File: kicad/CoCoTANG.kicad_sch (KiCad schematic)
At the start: 108 parts, among them J1 CPU, J10 PIA1_OUT, J13 CoCo_Cart, J14 PIA0_IN, J15 PIA1_IN, J17 AV_IN, J18 CMP_IN, J2 ADDRMUX_OUT, J20 AV_OUT, J21 CMP_OUT, J23 TRG, J28 ADDRMUX, J3 ADDRMUX_IN, J4 PIA0, J5 PIA1, J6 CLK, J7 AV_HEADER, J8 PIA0_OUT, Q1 MMBT3904-TP, Q2 MMBT3904-TP, Q3 MMBT3904-TP, Q4 MMBT3904-TP, Q5 MMBT3904-TP, Q6 MMBT3904-TP, Q7 MMBT3904-TP, Q8 MMBT3904-TP, Q9 MMBT3904-TP, U1 74HC138, U10 74LVC245, U11 74LVC245, U12 74LVC245, U2 AT28C64B-15PU, U22 74HC11, U3 74HC139, U5 Tang_Nano_20k, U7 74HC30, U8 74LVC245, U9 74HC245

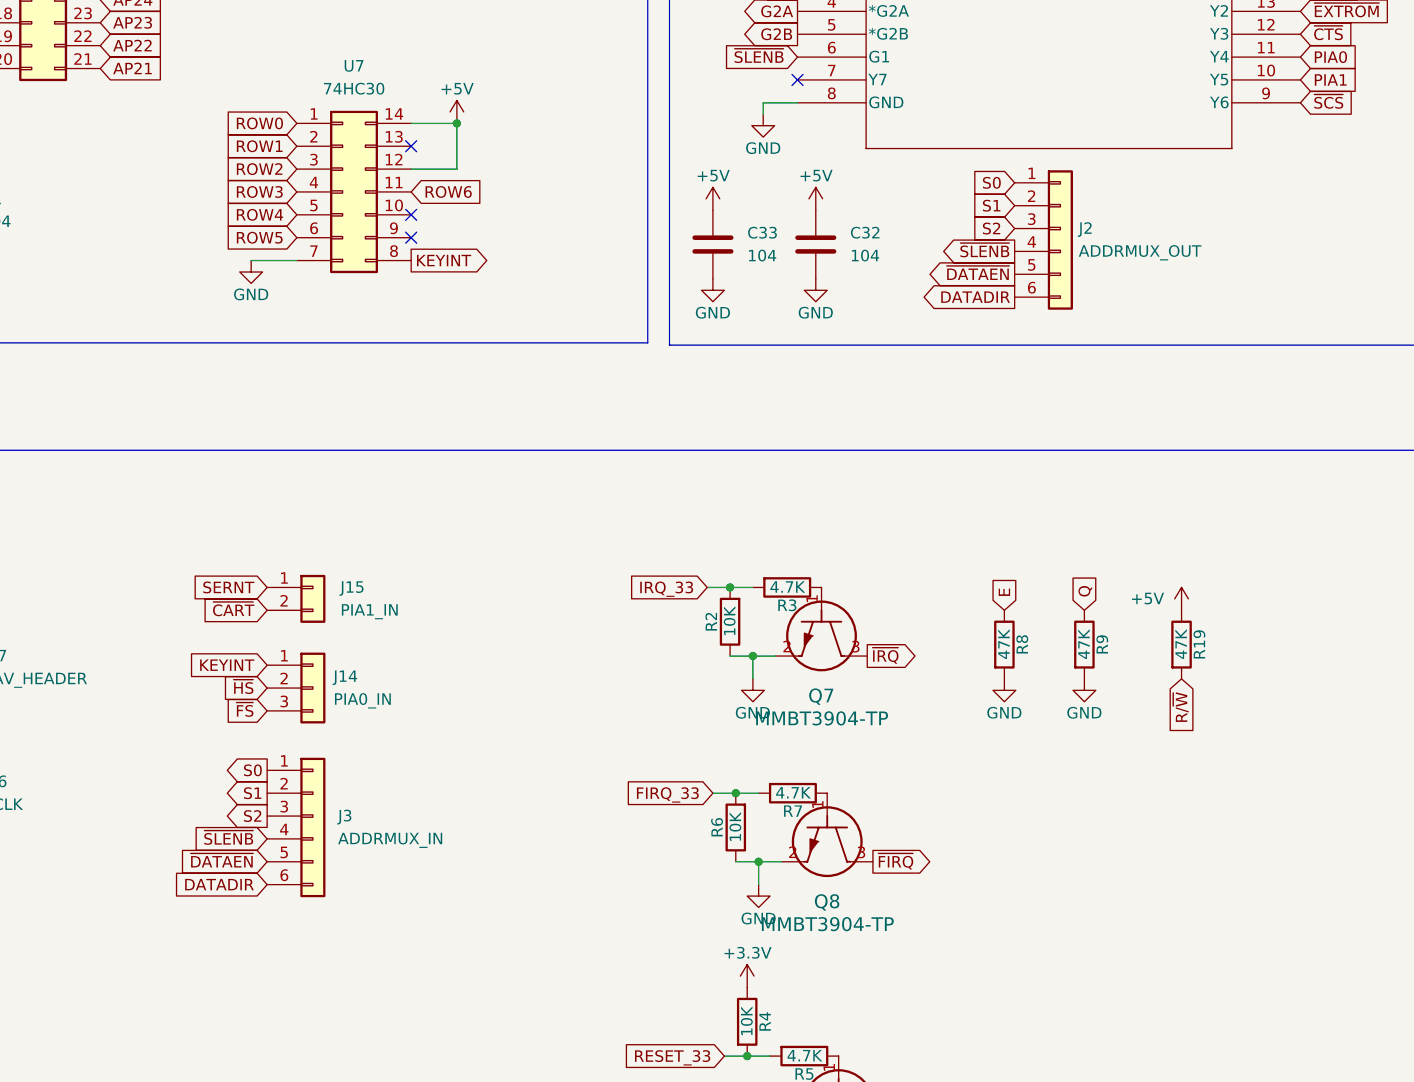
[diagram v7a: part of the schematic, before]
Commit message: fix missing board pin
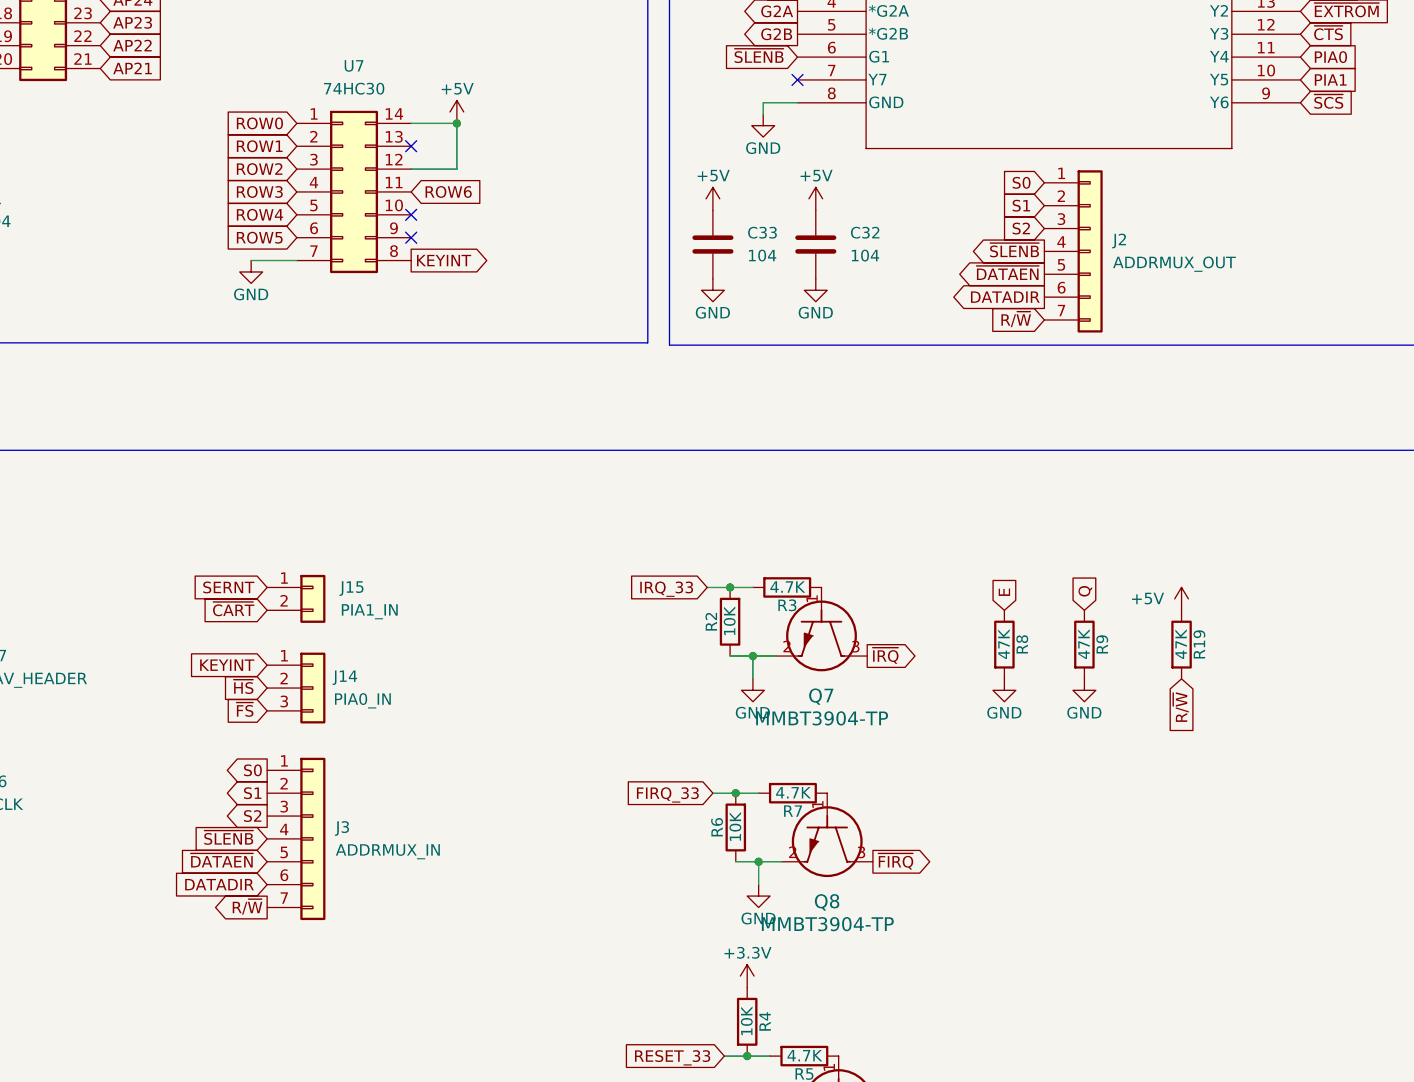
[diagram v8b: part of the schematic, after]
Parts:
- removed J2: ADDRMUX_OUT, Connector_PinHeader_2.54mm:PinHeader_1x06_P2.54mm_Vertical, symbol Connector_Generic:Conn_01x06
- removed J3: ADDRMUX_IN, Connector_PinHeader_2.54mm:PinHeader_1x06_P2.54mm_Vertical, symbol Connector_Generic:Conn_01x06
- added J2: ADDRMUX_OUT, Connector_PinHeader_2.54mm:PinHeader_1x07_P2.54mm_Vertical, symbol Connector_Generic:Conn_01x07
- added J3: ADDRMUX_IN, Connector_PinHeader_2.54mm:PinHeader_1x07_P2.54mm_Vertical, symbol Connector_Generic:Conn_01x07
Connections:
- net DATADIR: now also J2.6 (Pin_6), J3.6 (Pin_6)
- net R/~{W}: now also J2.7 (Pin_7), J3.7 (Pin_7)
- net S0: now also J2.1 (Pin_1), J3.1 (Pin_1)
- net S1: now also J2.2 (Pin_2), J3.2 (Pin_2)
- net S2: now also J2.3 (Pin_3), J3.3 (Pin_3)
- net ~{DATAEN}: now also J2.5 (Pin_5), J3.5 (Pin_5)
- net ~{SLENB}: now also J2.4 (Pin_4), J3.4 (Pin_4)
